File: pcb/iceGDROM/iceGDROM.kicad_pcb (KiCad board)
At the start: 4 copper layers, 100 x 35 mm, 116 parts, among them CN1 Molex_52602_0579, J1 Micro_SD_Card_Det_Hirose_DM3AT, J2 Conn_02x20_Odd_Even, J3 Conn_02x02_Odd_Even, J4 PMOD, J5 Conn_02x05_Odd_Even, SW1 SW_Push, SW2 SW_Push, SW3 SW_Push, U1 ICE40HX8K-BG121, U2 LD1117S12TR_SOT223, U3 ME6206A25M3G_SOT23, U4 W25Q32JVSS, X1 SG-310SCF

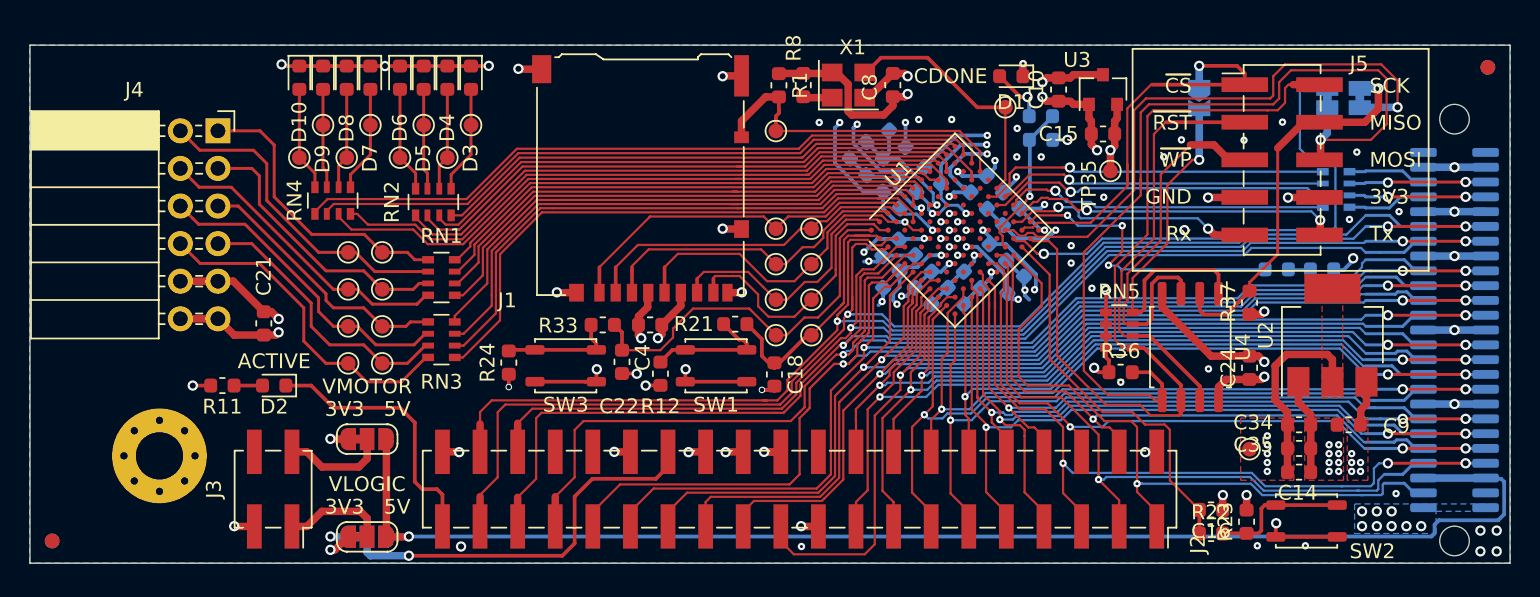
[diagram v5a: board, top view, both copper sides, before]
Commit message: Finalising the silkscreen & the schematic page
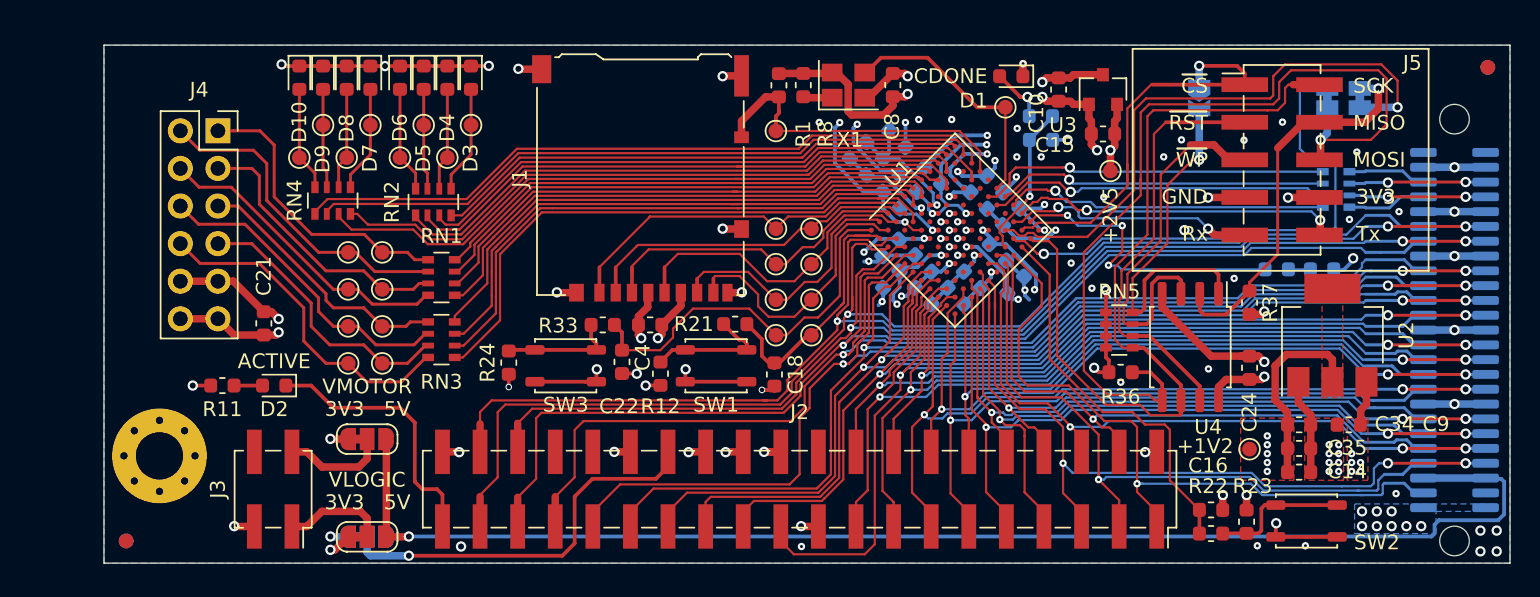
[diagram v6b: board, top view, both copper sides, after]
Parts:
- removed REF**: Symbol_GNU-Logo_SilkscreenTop, Symbol:Symbol_GNU-Logo_SilkscreenTop
- removed REF**: OSHW-Logo2_14.6x12mm_SilkScreen, Symbol:OSHW-Logo2_14.6x12mm_SilkScreen
- removed TP34: TestPoint, TestPoint:TestPoint_Pad_D1.0mm
- added +1V2: TestPoint, TestPoint:TestPoint_Pad_D1.0mm, F.Cu at (197.4, 97.3)
- J4: footprint iceGDROM:PMOD_Host_2x06_P2.54mm_Horizontal -> iceGDROM:PMOD_Host_2x06_P2.54mm_Vertical
- moved FID2 5.00 mm to (121.5, 103.5)
- moved FID4 5.00 mm to (121.5, 103.5)
- renumbered TP35 to +2V5
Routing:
- net GND: vias 91 -> 92
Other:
- board size 100 x 35 mm -> 95 x 35 mm
